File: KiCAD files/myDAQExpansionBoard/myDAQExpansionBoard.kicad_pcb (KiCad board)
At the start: 2 copper layers, 100 x 100 mm, 73 parts, among them J1 Conn_01x05_Male, J2 Conn_01x05_Male, J3 Conn_01x08_Male, J4 OSTV7XX3151, J5 Screw_Terminal_01x02, J6 Screw_Terminal_01x02, J7 Screw_Terminal_01x01, J8 Screw_Terminal_01x01, SW1 SW_SPDT, SW2 SW_SPDT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

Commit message: update
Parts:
- R1, R20: value 1k -> 4k7
- R10, R11, R13, R14, R15, R16, R8: value 680 -> 2k
- R5: value 1k -> 2k
- R7: value 1k -> 619
- R9: value 1k -> 6k8
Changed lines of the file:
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@@
       (effects (font (size 1 1) (thickness 0.15)))
     )
-    (fp_text value "1k" (at 0 1.43 -270) (layer "F.Fab")
+    (fp_text value "4k7" (at 0 1.43 -270) (layer "F.Fab")
       (effects (font (size 1 1) (thickness 0.15)))
     )
@@
       (effects (font (size 1 1) (thickness 0.15)))
     )
-    (fp_text value "680" (at 0 1.43) (layer "F.Fab")
+    (fp_text value "2k" (at 0 1.43) (layer "F.Fab")
       (effects (font (size 1 1) (thickness 0.15)))
     )
@@
       (effects (font (size 1 1) (thickness 0.15)))
     )
-    (fp_text value "680" (at 0 1.43) (layer "F.Fab")
+    (fp_text value "2k" (at 0 1.43) (layer "F.Fab")
       (effects (font (size 1 1) (thickness 0.15)))
     )
@@
       (effects (font (size 1 1) (thickness 0.15)))
     )
-    (fp_text value "680" (at 0 1.43) (layer "F.Fab")
+    (fp_text value "2k" (at 0 1.43) (layer "F.Fab")
       (effects (font (size 1 1) (thickness 0.15)))
     )
@@
       (effects (font (size 1 1) (thickness 0.15)))
     )
-    (fp_text value "1k" (at 0 1.43 90) (layer "F.Fab")
+    (fp_text value "619" (at 0 1.43 90) (layer "F.Fab")
       (effects (font (size 1 1) (thickness 0.15)))
     )
@@
       (effects (font (size 1 1) (thickness 0.15)))
     )
-    (fp_text value "1k" (at 0 1.43 90) (layer "F.Fab")
+    (fp_text value "2k" (at 0 1.43 90) (layer "F.Fab")
       (effects (font (size 1 1) (thickness 0.15)))
     )
@@
       (effects (font (size 1 1) (thickness 0.15)))
     )
-    (fp_text value "1k" (at 0 1.43 90) (layer "F.Fab")
+    (fp_text value "6k8" (at 0 1.43 90) (layer "F.Fab")
       (effects (font (size 1 1) (thickness 0.15)))
     )
@@
       (effects (font (size 1 1) (thickness 0.15)))
     )
-    (fp_text value "1k" (at 0 1.43 90) (layer "F.Fab")
+    (fp_text value "4k7" (at 0 1.43 90) (layer "F.Fab")
       (effects (font (size 1 1) (thickness 0.15)))
     )
@@
       (effects (font (size 1 1) (thickness 0.15)))
     )
-    (fp_text value "680" (at 0 1.43) (layer "F.Fab")
+    (fp_text value "2k" (at 0 1.43) (layer "F.Fab")
       (effects (font (size 1 1) (thickness 0.15)))
     )
@@
       (effects (font (size 1 1) (thickness 0.15)))
     )
-    (fp_text value "680" (at 0 1.43) (layer "F.Fab")
+    (fp_text value "2k" (at 0 1.43) (layer "F.Fab")
       (effects (font (size 1 1) (thickness 0.15)))
     )
@@
       (effects (font (size 1 1) (thickness 0.15)))
     )
-    (fp_text value "680" (at 0 1.43) (layer "F.Fab")
+    (fp_text value "2k" (at 0 1.43) (layer "F.Fab")
       (effects (font (size 1 1) (thickness 0.15)))
     )
@@
       (effects (font (size 1 1) (thickness 0.15)))
     )
-    (fp_text value "680" (at 0 1.43) (layer "F.Fab")
+    (fp_text value "2k" (at 0 1.43) (layer "F.Fab")
       (effects (font (size 1 1) (thickness 0.15)))
     )

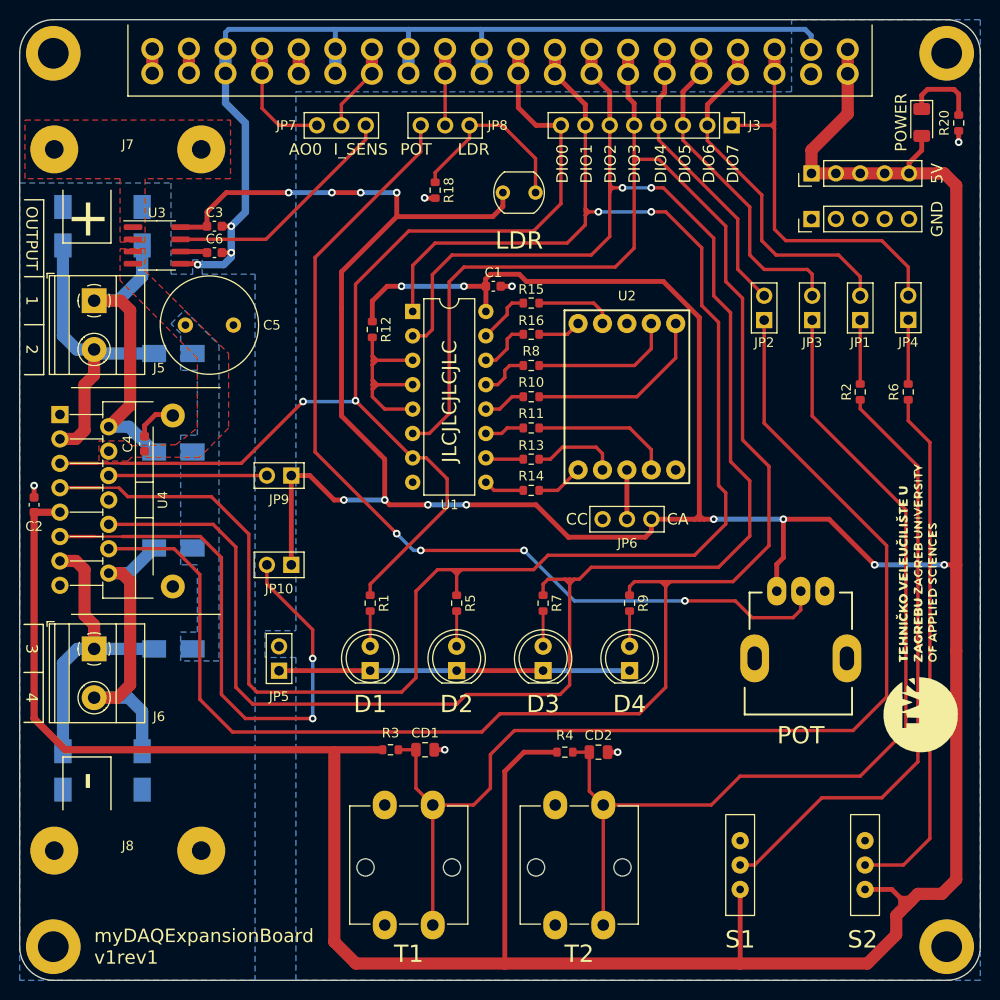
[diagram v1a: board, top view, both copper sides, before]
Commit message: Added resistor for RC circuit
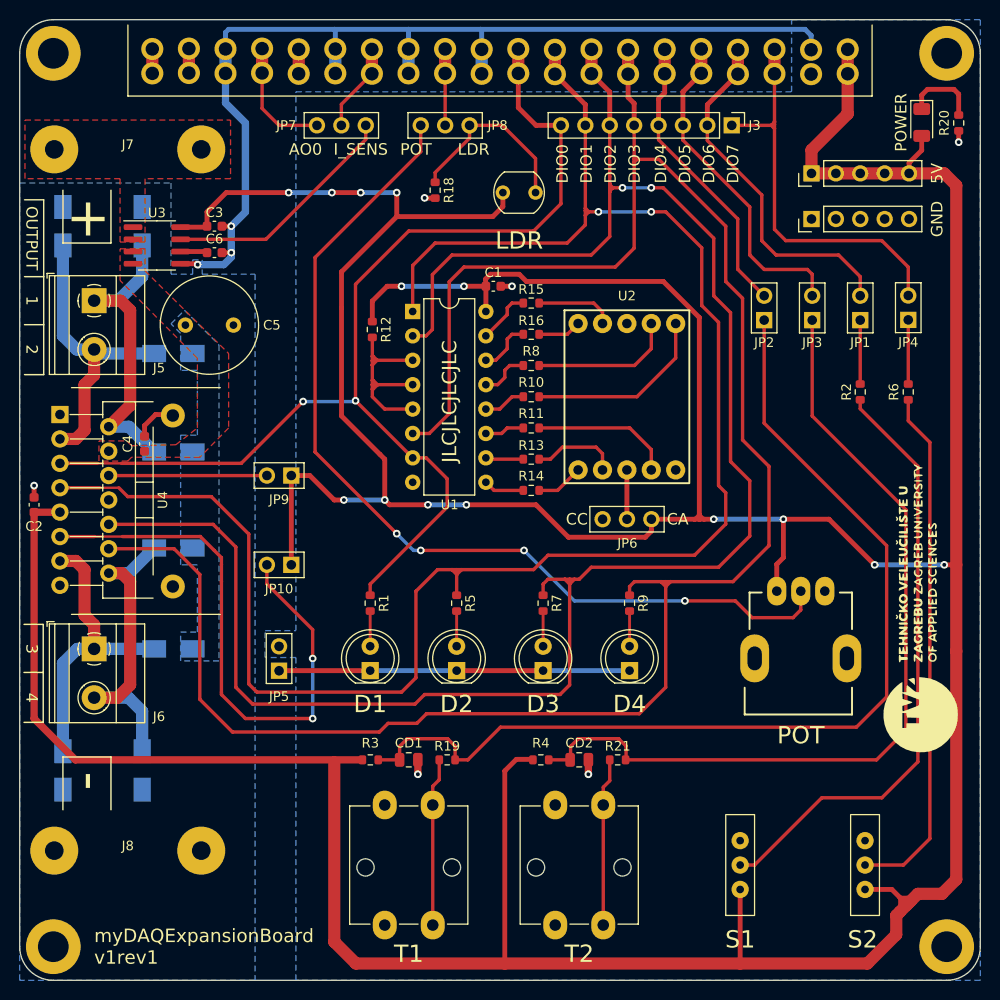
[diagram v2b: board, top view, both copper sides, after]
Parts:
- added R19: 1k, Resistor_SMD:R_0603_1608Metric, F.Cu at (113.8, 110.8)
- added R21: 1k, Resistor_SMD:R_0603_1608Metric, F.Cu at (131.5, 110.8)
- moved R4 2.62 mm to (123.5, 110.8)
- moved R3 2.35 mm to (105.8, 110.8)
- moved CD2 2.15 mm to (127.5, 110.8)
- moved CD1 2.00 mm to (109.8, 110.8)
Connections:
- CD1 pad 1: Net-(CD1-Pad1) -> Net-(JP2-Pad1)
- CD2 pad 1: Net-(CD2-Pad1) -> Net-(JP3-Pad1)
- JP2 pad 1: Net-(CD1-Pad1) -> Net-(JP2-Pad1)
- JP3 pad 1: Net-(CD2-Pad1) -> Net-(JP3-Pad1)
- R3 pad 2: Net-(CD1-Pad1) -> Net-(JP2-Pad1)
- R4 pad 2: Net-(CD2-Pad1) -> Net-(JP3-Pad1)
- SW3 pad 1: Net-(CD1-Pad1) -> Net-(R19-Pad1)
- SW4 pad 1: Net-(CD2-Pad1) -> Net-(SW4-Pad1)
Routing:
- net Net-(CD1-Pad1): track 119.3 -> 0.00 mm
- net Net-(JP2-Pad1): track 0.00 -> 103.6 mm
- net Net-(CD2-Pad1): track 101.8 -> 0.00 mm
- net Net-(JP3-Pad1): track 0.00 -> 88.7 mm
- net Net-(SW4-Pad1): track 0.00 -> 17.5 mm
- net Net-(R19-Pad1): track 0.00 -> 17.5 mm
- net +5V: track 531.5 -> 526.1 mm
- net GND: track 119.6 -> 120.4 mm

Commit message: update
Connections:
- JP2 pad 2: DIO4 -> DIO0
- JP3 pad 2: DIO5 -> DIO2
- JP4 pad 2: DIO7 -> DIO4
- R1 pad 1: DIO0 -> DIO1
- R5 pad 1: DIO1 -> DIO3
- R7 pad 1: DIO2 -> DIO5
- R9 pad 1: DIO3 -> DIO7
- U1 pad 1: DIO1 -> DIO3
- U1 pad 2: DIO2 -> DIO5
- U1 pad 6: DIO3 -> DIO7
- U1 pad 7: DIO0 -> DIO1
- U4 pad 10: DIO2 -> DIO5
- U4 pad 12: DIO3 -> DIO7
- U4 pad 5: DIO0 -> DIO3
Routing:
- net DIO5: track 34.7 -> 191.7 mm, vias 0 -> 2
- net DIO2: track 197.4 -> 47.6 mm
- net DIO7: track 42.7 -> 185.6 mm
- net DIO3: track 213.6 -> 139.2 mm, vias 0 -> 6
- net DIO0: track 118.3 -> 45.5 mm, vias 2 -> 3
- net DIO1: track 192.4 -> 134.1 mm, vias 2 -> 3
- net DIO4: track 30.5 -> 54.2 mm
- net Net-(JP8-Pad1): track 98.5 -> 114.6 mm, vias 4 -> 2
- net DIO6: track 37.3 -> 43.8 mm
- net +5V: track 526.1 -> 528.0 mm
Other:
- board text added: "ENC1_A/DIO4"
- board text added: "ENC1_B/DIO6"
- board text added: "ENCO_A/DIO0"
- board text added: "ENCO_B/DIO2"
- board text added: "PWM0/DIO3"
- board text added: "PWM1/DIO7"
- board text removed: "DIO0"
- board text removed: "DIO2"
- board text removed: "DIO3"
- board text removed: "DIO4"
- board text removed: "DIO6"
- board text removed: "DIO7"

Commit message: v1rev2
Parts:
- SW1, SW2: footprint Library:we01014042 -> Library:500SSP1S1M2QEA
- turned SW1 to 180 degrees
- turned SW2 to 180 degrees
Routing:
- net Net-(R2-Pad1): track 63.1 -> 66.2 mm
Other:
- board text added: "myDAQExpansionBoard v1rev2"
- board text removed: "myDAQExpansionBoard v1rev1"

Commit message: update
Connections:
- JP1 pad 2: DIO6 -> DIO0
- JP2 pad 2: DIO0 -> DIO6
- JP3 pad 2: DIO2 -> DIO4
- JP4 pad 2: DIO4 -> DIO2
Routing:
- net DIO4: track 54.2 -> 37.8 mm, vias 0 -> 2
- net DIO2: track 47.6 -> 59.8 mm, vias 2 -> 0
- net DIO0: track 45.5 -> 55.2 mm, vias 3 -> 4
- net DIO6: track 43.8 -> 36.8 mm
- net Net-(CD1-Pad1): track 103.8 -> 105.6 mm
- net Net-(CD2-Pad1): track 88.7 -> 87.6 mm
- net Net-(R2-Pad1): track 66.2 -> 65.5 mm
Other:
- board text added: "myDAQ/myRIO ExpansionBoard v1rev2"
- board text removed: "myDAQExpansionBoard v1rev2"

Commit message: update
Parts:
- SW1, SW2: footprint Library:500SSP1S1M2QEA -> Library:EG1271A
- turned SW1 to -90 degrees
- turned SW2 to -90 degrees
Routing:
- net +5V: track 528.1 -> 546.3 mm
- net Net-(R2-Pad1): track 65.5 -> 75.7 mm
- net Net-(R6-Pad2): track 54.7 -> 56.3 mm
